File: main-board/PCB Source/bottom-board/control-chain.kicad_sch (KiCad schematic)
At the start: 14 parts, among them P13 RJ45, U12 ISL83491

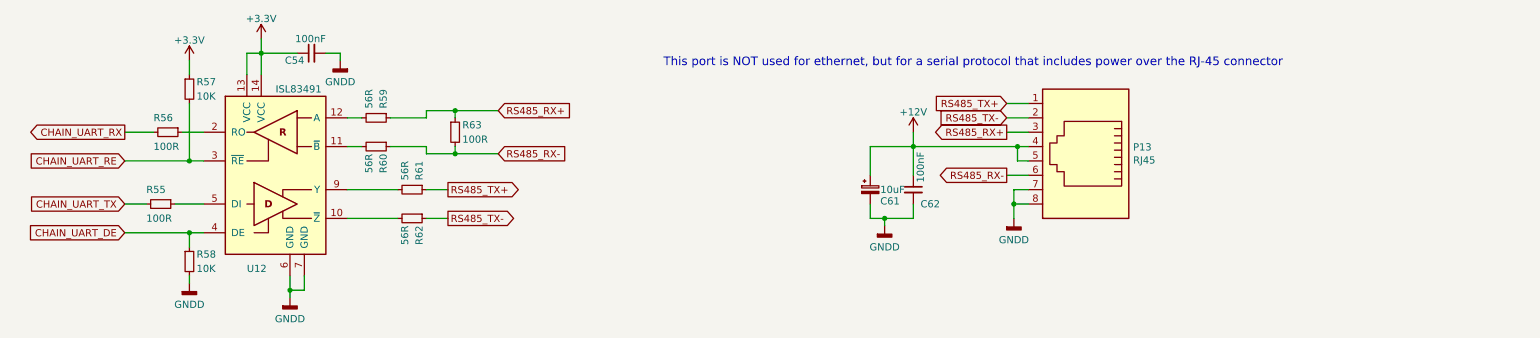
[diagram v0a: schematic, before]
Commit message: mainboard: add bias buffer, update MPNs, clean schematic
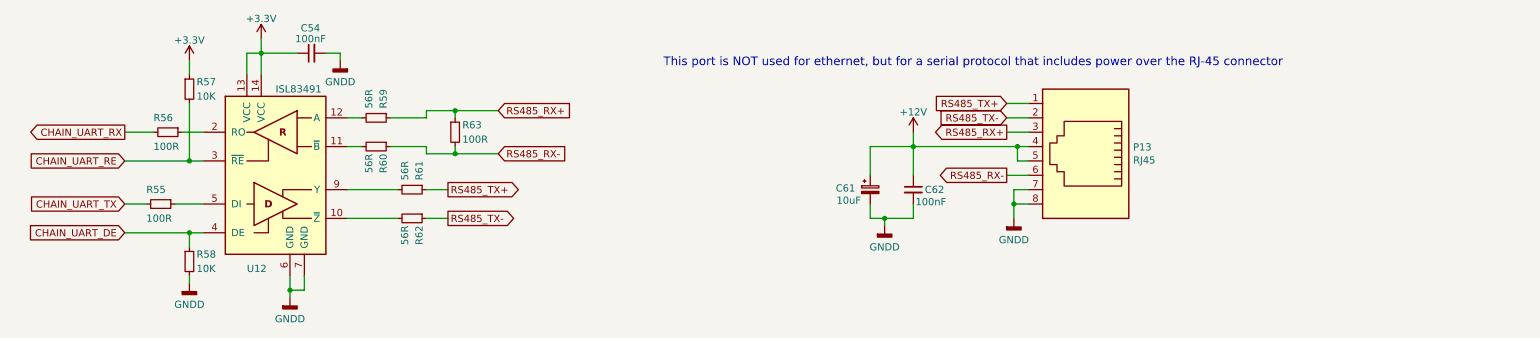
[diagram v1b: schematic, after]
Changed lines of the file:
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@@
     (title "MOD Dwarf - Main Board")
     (date "2021-09-06")
-    (rev "1.3")
+    (rev "3.0")
     (company "MOD Devices GmbH")
     (comment 1 "Dwarf Audio processing board")
@@
   (symbol (lib_id "bottom-board-rescue:C_Small") (at 89.281 65.024 90) (mirror x) (unit 1)
     (in_bom yes) (on_board yes)
-    (property "Reference" "C54" (id 0) (at 88.011 66.294 90)
+    (property "Reference" "C54" (id 0) (at 90.805 60.579 90)
       (effects (font (size 1.27 1.27)) (justify left))
     )
@@
   (symbol (lib_id "bottom-board-rescue:C_Small") (at 195.707 89.154 0) (unit 1)
     (in_bom yes) (on_board yes)
-    (property "Reference" "C62" (id 0) (at 196.977 91.694 0)
-      (effects (font (size 1.27 1.27)) (justify left))
-    )
-    (property "Value" "100nF" (id 1) (at 196.977 87.884 90)
+    (property "Reference" "C62" (id 0) (at 197.739 89.154 0)
+      (effects (font (size 1.27 1.27)) (justify left))
+    )
+    (property "Value" "100nF" (id 1) (at 196.088 91.313 0)
       (effects (font (size 1.27 1.27)) (justify left))
     )
@@
   (symbol (lib_id "bottom-board-rescue:CP_Small") (at 188.087 89.154 0) (unit 1)
     (in_bom yes) (on_board yes)
-    (property "Reference" "C61" (id 0) (at 189.865 91.186 0)
-      (effects (font (size 1.27 1.27)) (justify left))
-    )
-    (property "Value" "10uF" (id 1) (at 189.865 89.154 0)
-      (effects (font (size 1.27 1.27)) (justify left))
-    )
+    (property "Reference" "C61" (id 0) (at 181.991 88.9 0)
+      (effects (font (size 1.27 1.27)) (justify left))
+    )
+    (property "Value" "10uF" (id 1) (at 182.118 91.059 0)
+      (effects (font (size 1.27 1.27)) (justify left))
+    )
